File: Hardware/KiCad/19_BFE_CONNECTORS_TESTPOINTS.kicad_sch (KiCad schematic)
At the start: 0 parts

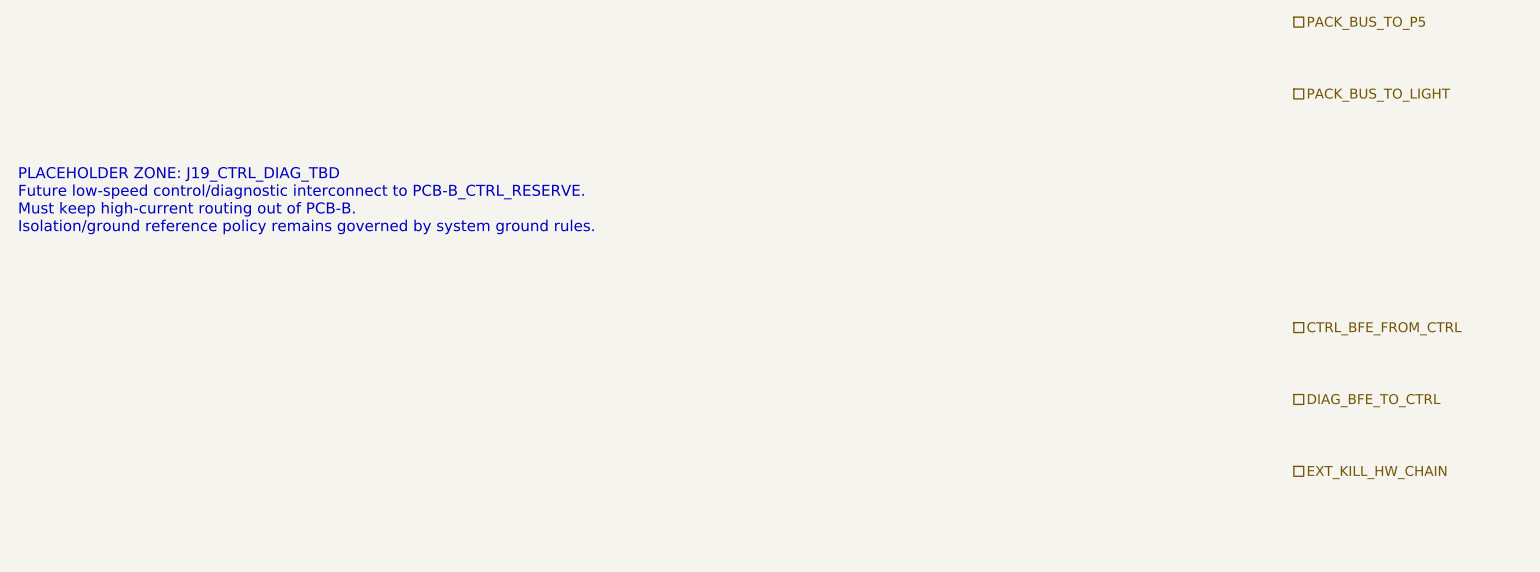
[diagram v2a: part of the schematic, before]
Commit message: hardware: align PCB-A connector group names
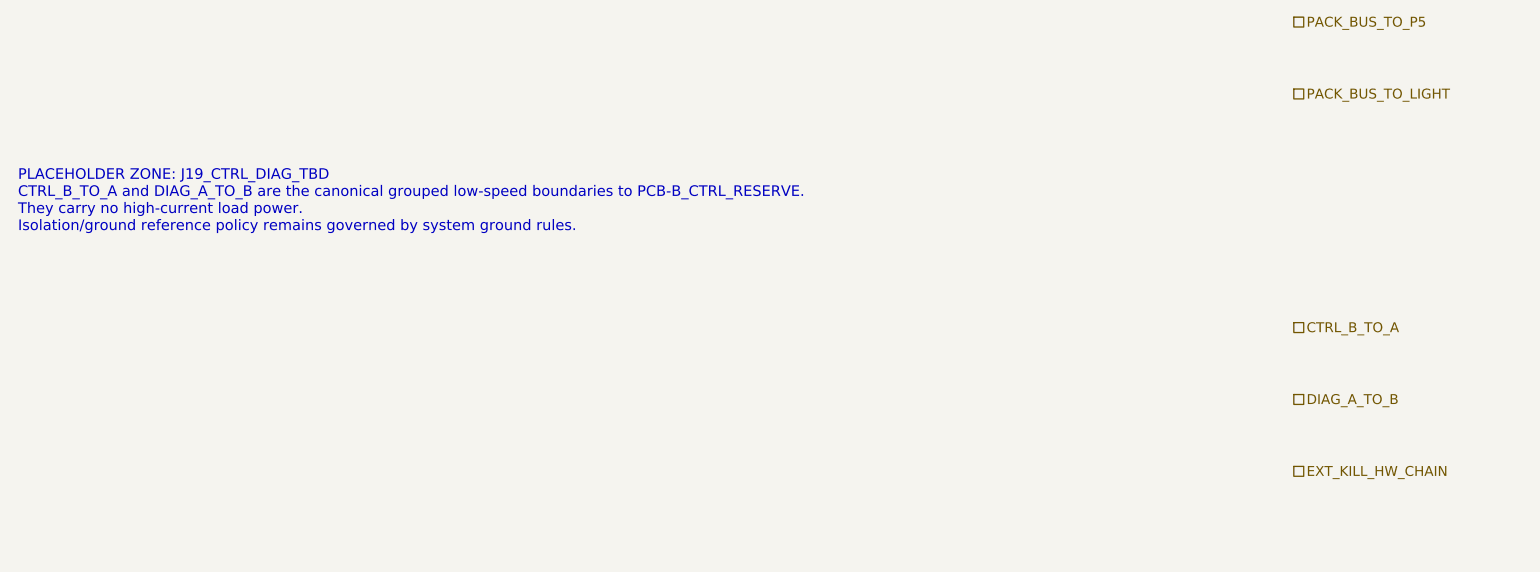
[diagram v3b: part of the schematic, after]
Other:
- note added: "PLACEHOLDER ZONE: J19_CTRL_DIAG_TBD CTRL_B_TO_A and DIAG_A_TO_B are the canonical grouped low-speed boundaries to PCB-B_CTRL_RESERVE. They carry no high-current load power. Isolation/ground reference policy remains governed by system ground rules."
- note removed: "PLACEHOLDER ZONE: J19_CTRL_DIAG_TBD Future low-speed control/diagnostic interconnect to PCB-B_CTRL_RESERVE. Must keep high-current routing out of PCB-B. Isolation/ground reference policy remains governed by system ground rules."
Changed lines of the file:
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@@
 		(title "19_BFE_CONNECTORS_TESTPOINTS - BFE connector/test boundary")
 		(date "2026-07-15")
-		(rev "C1")
+		(rev "C2")
 		(company "Gonoboben/plataVM")
-		(comment 1 "Symbol skeleton: BFE connector groups and protected testpoint placeholders")
+		(comment 1 "Interface consistency: canonical CTRL_B_TO_A and DIAG_A_TO_B connector groups")
 		(comment 2 "No connector family, pin count, wire section, footprint or BOM part selected")
 	)
@@
 		(uuid "bfe-lb-00000019-0000-4000-8000-000000000102")
 	)
-	(text "PLACEHOLDER ZONE: J19_CTRL_DIAG_TBD\nFuture low-speed control/diagnostic interconnect to PCB-B_CTRL_RESERVE.\nMust keep high-current routing out of PCB-B.\nIsolation/ground reference policy remains governed by system ground rules."
+	(text "PLACEHOLDER ZONE: J19_CTRL_DIAG_TBD\nCTRL_B_TO_A and DIAG_A_TO_B are the canonical grouped low-speed boundaries to PCB-B_CTRL_RESERVE.\nThey carry no high-current load power.\nIsolation/ground reference policy remains governed by system ground rules."
 		(exclude_from_sim no)
 		(at 12 120 0)
-		(effects (font (size 1.22 1.22)) (justify left))
+		(effects (font (size 1.18 1.18)) (justify left))
 		(uuid "bfe-lb-00000019-0000-4000-8000-000000000103")
 	)
@@
 	(hierarchical_label "PACK_BUS_TO_P5" (shape passive) (exclude_from_sim no) (at 154 100 0) (effects (font (size 1.1 1.1)) (justify left)) (uuid "bfe-lb-00000019-0000-4000-8000-000000000203"))
 	(hierarchical_label "PACK_BUS_TO_LIGHT" (shape passive) (exclude_from_sim no) (at 154 108 0) (effects (font (size 1.1 1.1)) (justify left)) (uuid "bfe-lb-00000019-0000-4000-8000-000000000204"))
-	(hierarchical_label "CTRL_BFE_FROM_CTRL" (shape passive) (exclude_from_sim no) (at 154 134 0) (effects (font (size 1.1 1.1)) (justify left)) (uuid "bfe-lb-00000019-0000-4000-8000-000000000205"))
-	(hierarchical_label "DIAG_BFE_TO_CTRL" (shape passive) (exclude_from_sim no) (at 154 142 0) (effects (font (size 1.1 1.1)) (justify left)) (uuid "bfe-lb-00000019-0000-4000-8000-000000000206"))
+	(hierarchical_label "CTRL_B_TO_A" (shape passive) (exclude_from_sim no) (at 154 134 0) (effects (font (size 1.1 1.1)) (justify left)) (uuid "bfe-lb-00000019-0000-4000-8000-000000000205"))
+	(hierarchical_label "DIAG_A_TO_B" (shape passive) (exclude_from_sim no) (at 154 142 0) (effects (font (size 1.1 1.1)) (justify left)) (uuid "bfe-lb-00000019-0000-4000-8000-000000000206"))
 	(hierarchical_label "EXT_KILL_HW_CHAIN" (shape passive) (exclude_from_sim no) (at 154 150 0) (effects (font (size 1.1 1.1)) (justify left)) (uuid "bfe-lb-00000019-0000-4000-8000-000000000207"))
 	(hierarchical_label "BFE_TP_LOW_ENERGY" (shape passive) (exclude_from_sim no) (at 154 184 0) (effects (font (size 1.1 1.1)) (justify left)) (uuid "bfe-lb-00000019-0000-4000-8000-000000000208"))
